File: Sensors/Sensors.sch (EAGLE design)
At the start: 43 parts, among them IC1 MAX31855, IC2 MAX31855, IC3 MAX31855

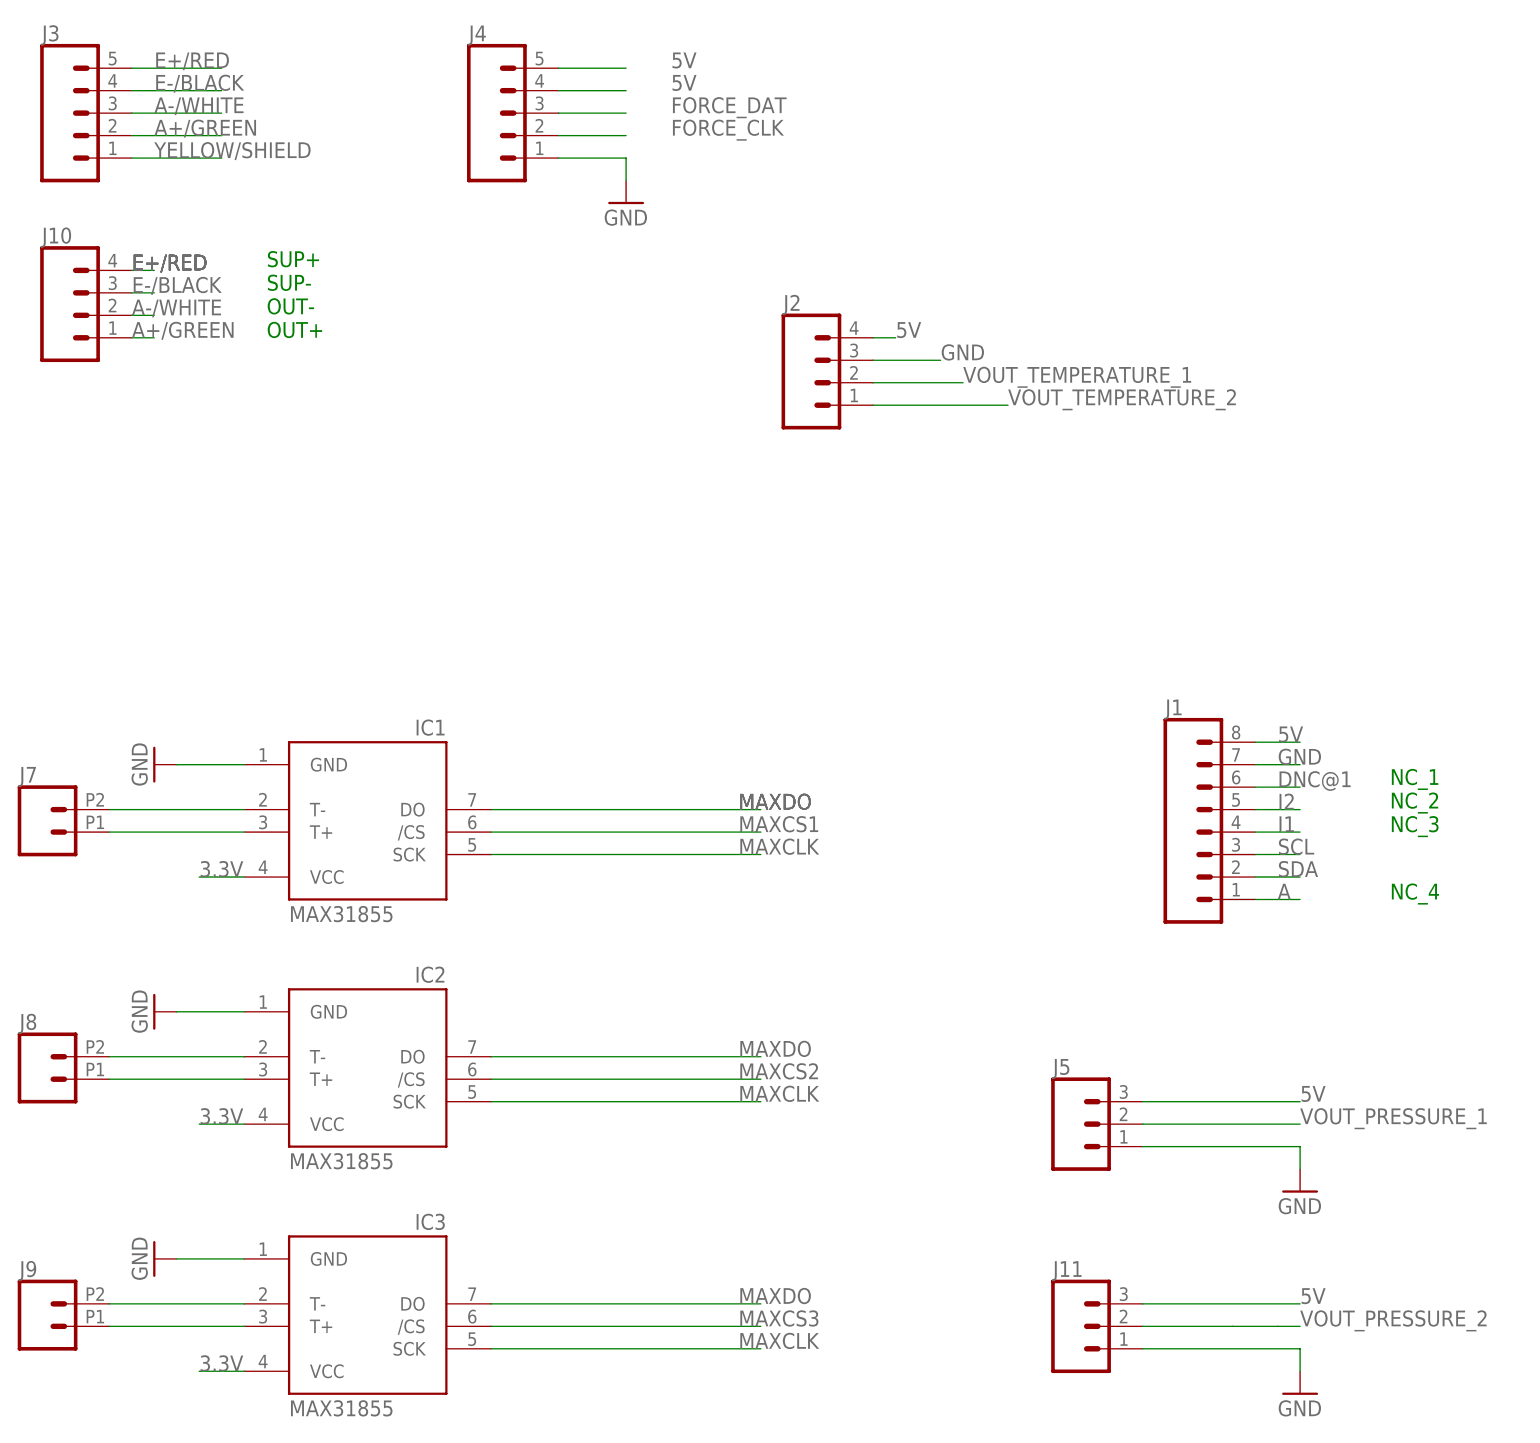
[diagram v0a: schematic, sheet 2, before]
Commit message: Removed thermocouples, added JSTs
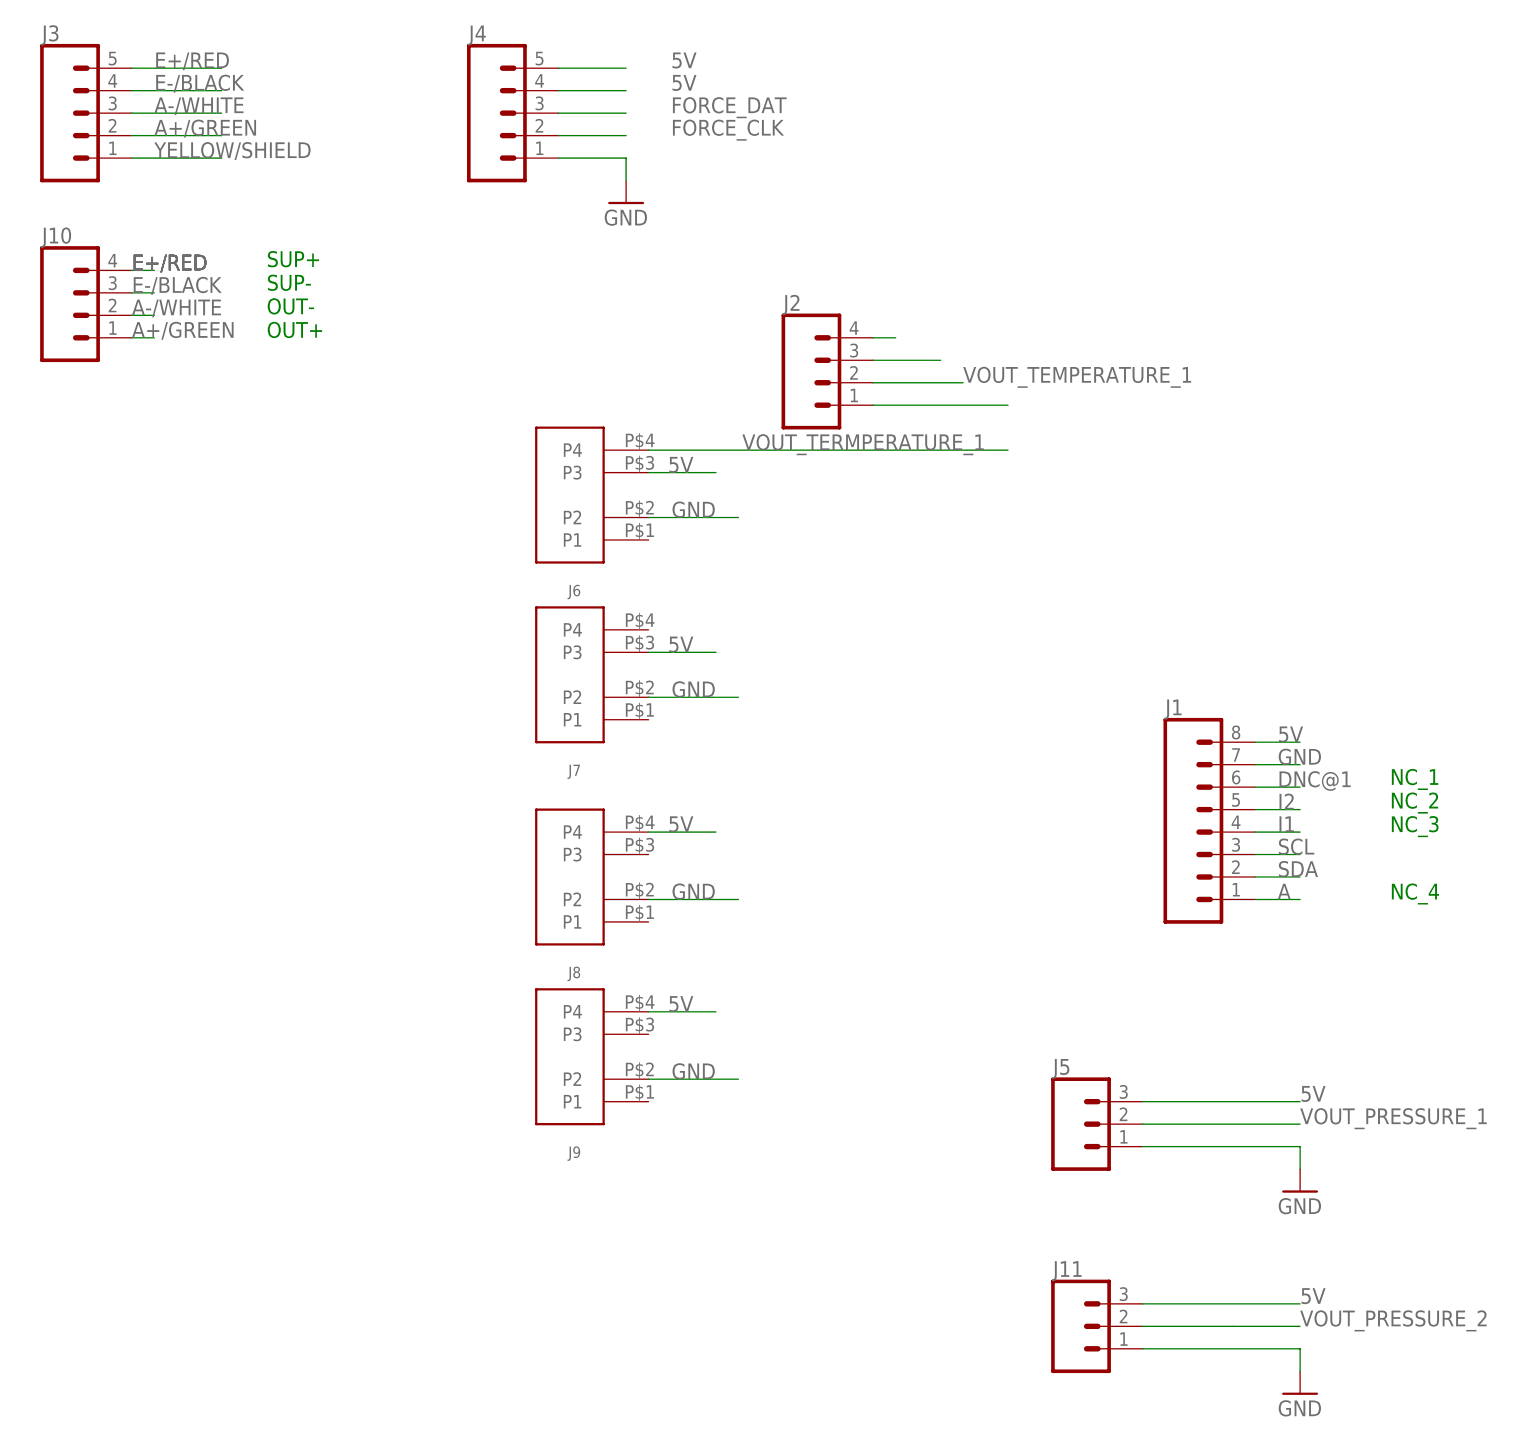
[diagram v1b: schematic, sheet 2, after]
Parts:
- removed IC1, IC2, IC3: MAX31855, adafruit:MAX6675
- removed LED1, LED2, LED3: (no value), adafruit:LEDCHIP-LED0805
- removed R1, R2, R3: 1000, resistor:R-US_R0805
- added J6: JST_CONNECTOR, LPRD_RELAY:JST_CONNECTOR
- J7, J8, J9: value (none) -> JST_CONNECTOR; device SparkFun-Connectors:CONN_022.54MM_SCREWTERM -> LPRD_RELAY:JST_CONNECTOR
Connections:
- removed net D20: JP5.2
- removed net D21: JP5.1
- removed net N$1: LED1.A, R1.2
- removed net N$10: IC1.T+, J7.1
- removed net N$11: IC2.T-, J8.2
- removed net N$12: IC2.T+, J8.1
- removed net N$13: IC3.T-, J9.2
- removed net N$14: IC3.T+, J9.1
- removed net N$2: LED2.A, R2.2
- removed net N$3: LED3.A, R3.2
- removed net N$8: IC1.T-, J7.2
- new net VOUT_TERMPERATURE_1: J6.P4
- net 3.3V: no longer IC1.VCC, IC2.VCC, IC3.VCC
- net 5V: now also J6.P3, J7.P3, J8.P4, J9.P4
- net GND: now also J6.P2, J7.P2, J8.P2, J9.P2; no longer IC1.GND, IC2.GND, IC3.GND, LED1.C, LED2.C, LED3.C
- net MAXCLK: no longer IC1.SCK, IC2.SCK, IC3.SCK
- net MAXCS1: no longer IC1./CS
- net MAXCS2: no longer IC2./CS
- net MAXCS3: no longer IC3./CS
- net MAXDO: no longer IC1.DO, IC2.DO, IC3.DO
- net SCL: now also JP5.1; no longer JP5.8
- net SDA: now also JP5.2; no longer JP5.7
- net THERMO1_LED: no longer R1.1
- net THERMO2_LED: no longer R2.1
- net THERMO3_LED: no longer R3.1
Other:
- moved on the sheet: LED10, LED8, LED9, R10, R8, R9

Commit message: Updated Schematic, pins now aligned and connected
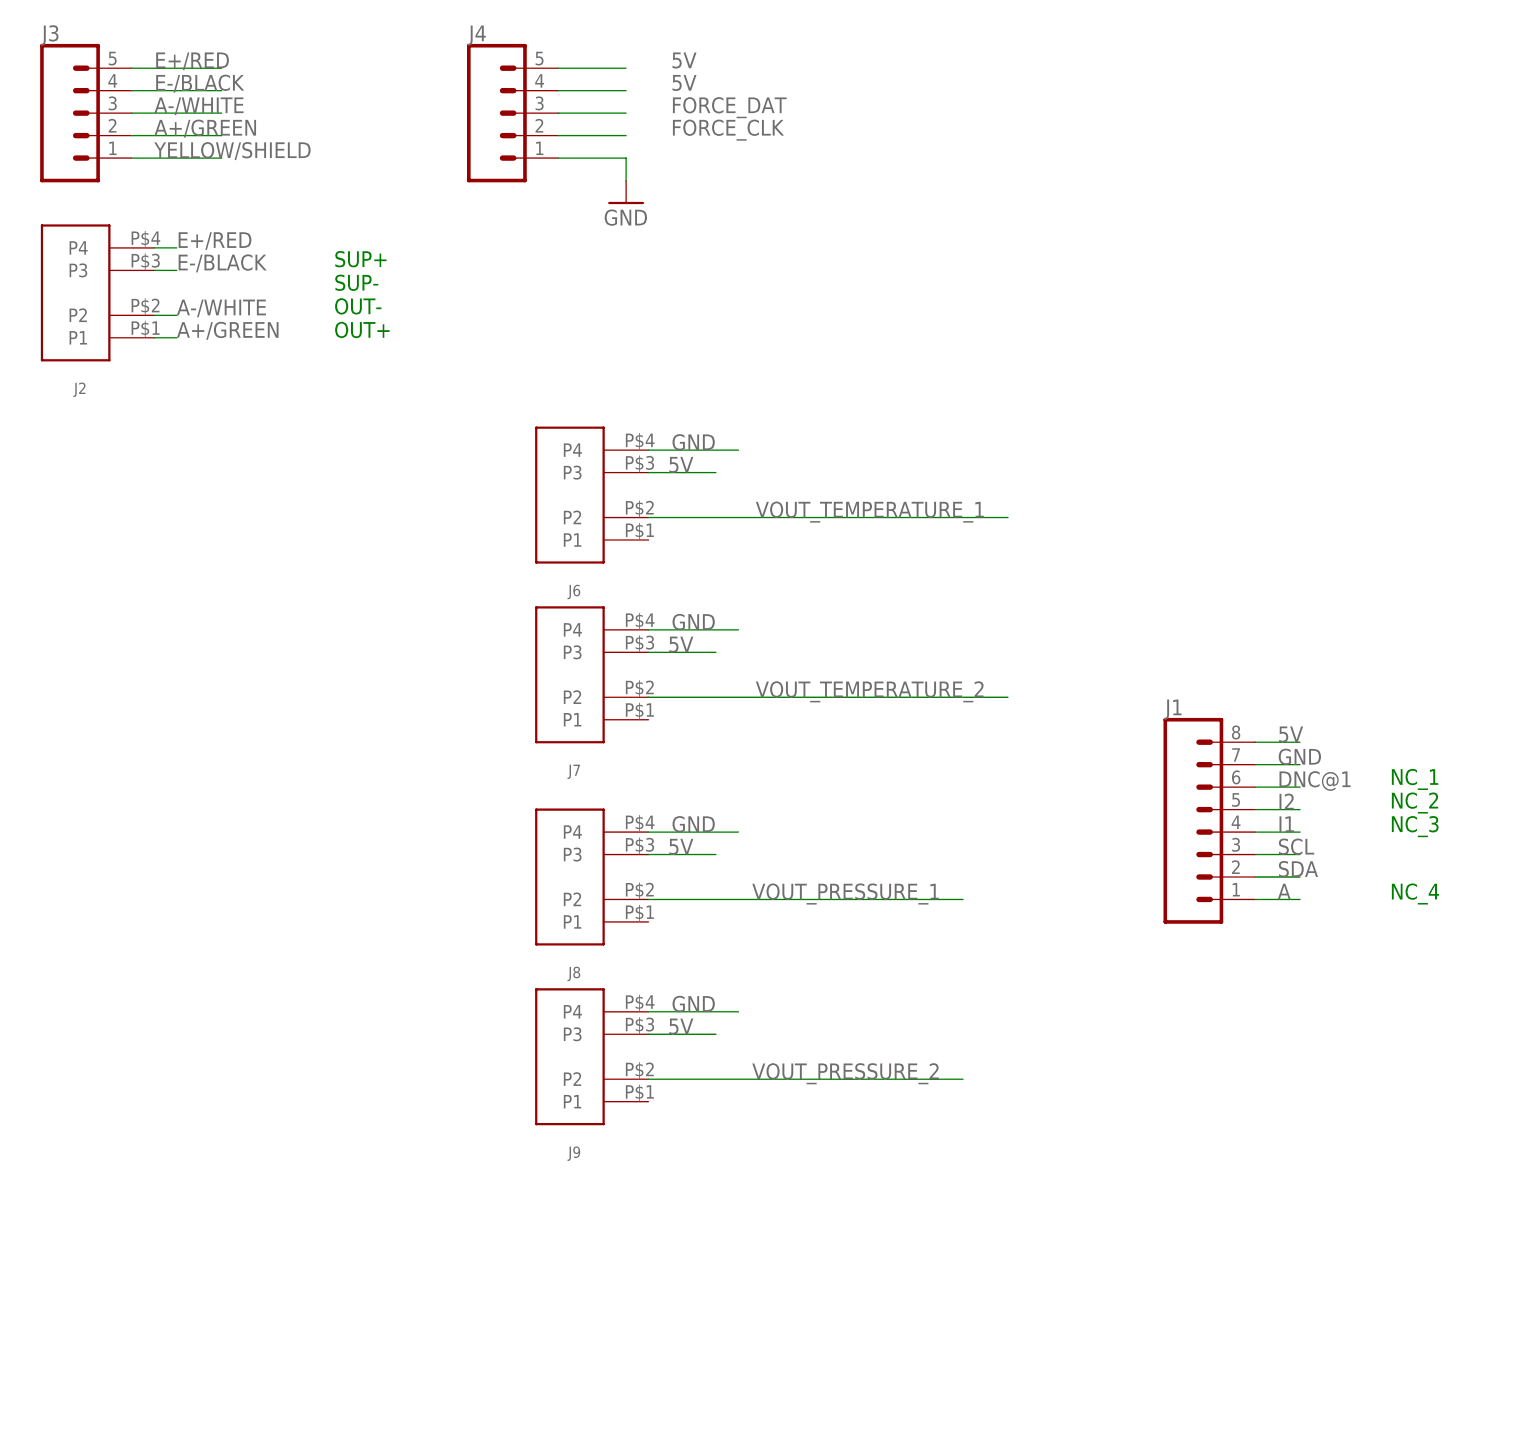
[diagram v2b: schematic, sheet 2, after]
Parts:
- removed J10: (no value), SparkFun-Connectors:CONN_04SCREW
- removed J11, J5: (no value), SparkFun-Connectors:CONN_03-SCREW-5MM
- J2: value (none) -> JST_CONNECTOR; device SparkFun-Connectors:CONN_04 -> LPRD_RELAY:JST_CONNECTOR
- LED10, LED4, LED5, LED6, LED7, LED8, LED9: device adafruit:LEDCHIP-LED0805 -> led:LED3MM
- R10, R4, R5, R6, R7, R8, R9: device resistor:R-US_R0805 -> rcl:R-US_0204/7
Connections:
- net MAXCS2 renamed D33
- net MAXCS3 renamed D31
- net THERMO1_LED renamed D46
- net THERMO2_LED renamed D44
- net THERMO3_LED renamed D42
- removed net VOUT_TERMPERATURE_1: J6.P4
- net 5V: now also J8.P3, J9.P3; no longer J11.3, J2.4, J5.3, J8.P4, J9.P4
- net A+/GREEN: now also J2.P1; no longer J10.1
- net A-/WHITE: now also J2.P2; no longer J10.2
- net E+/RED: now also J2.P4; no longer J10.4
- net E-/BLACK: now also J2.P3; no longer J10.3
- net GND: now also J6.P4, J7.P4, J8.P4, J9.P4; no longer J11.1, J2.3, J5.1, J6.P2, J7.P2, J8.P2, J9.P2
- net VOUT_PRESSURE_1: now also J8.P2; no longer J5.2
- net VOUT_PRESSURE_2: now also J9.P2; no longer J11.2
- net VOUT_TEMPERATURE_1: now also J6.P2; no longer J2.2
- net VOUT_TEMPERATURE_2: now also J7.P2; no longer J2.1
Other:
- moved on the sheet: J2
